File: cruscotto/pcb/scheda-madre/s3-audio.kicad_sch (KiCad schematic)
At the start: 11 parts, among them J10 Verso P1 S3: 5V TXD RXD GND, J11 Verso P2 S3: IO19 IO11 IO12 I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, J12 Verso P6 Speak S3, K1 G2RL-2 DC5, K2 G2RL-2 DC5, Q9 AO3400A

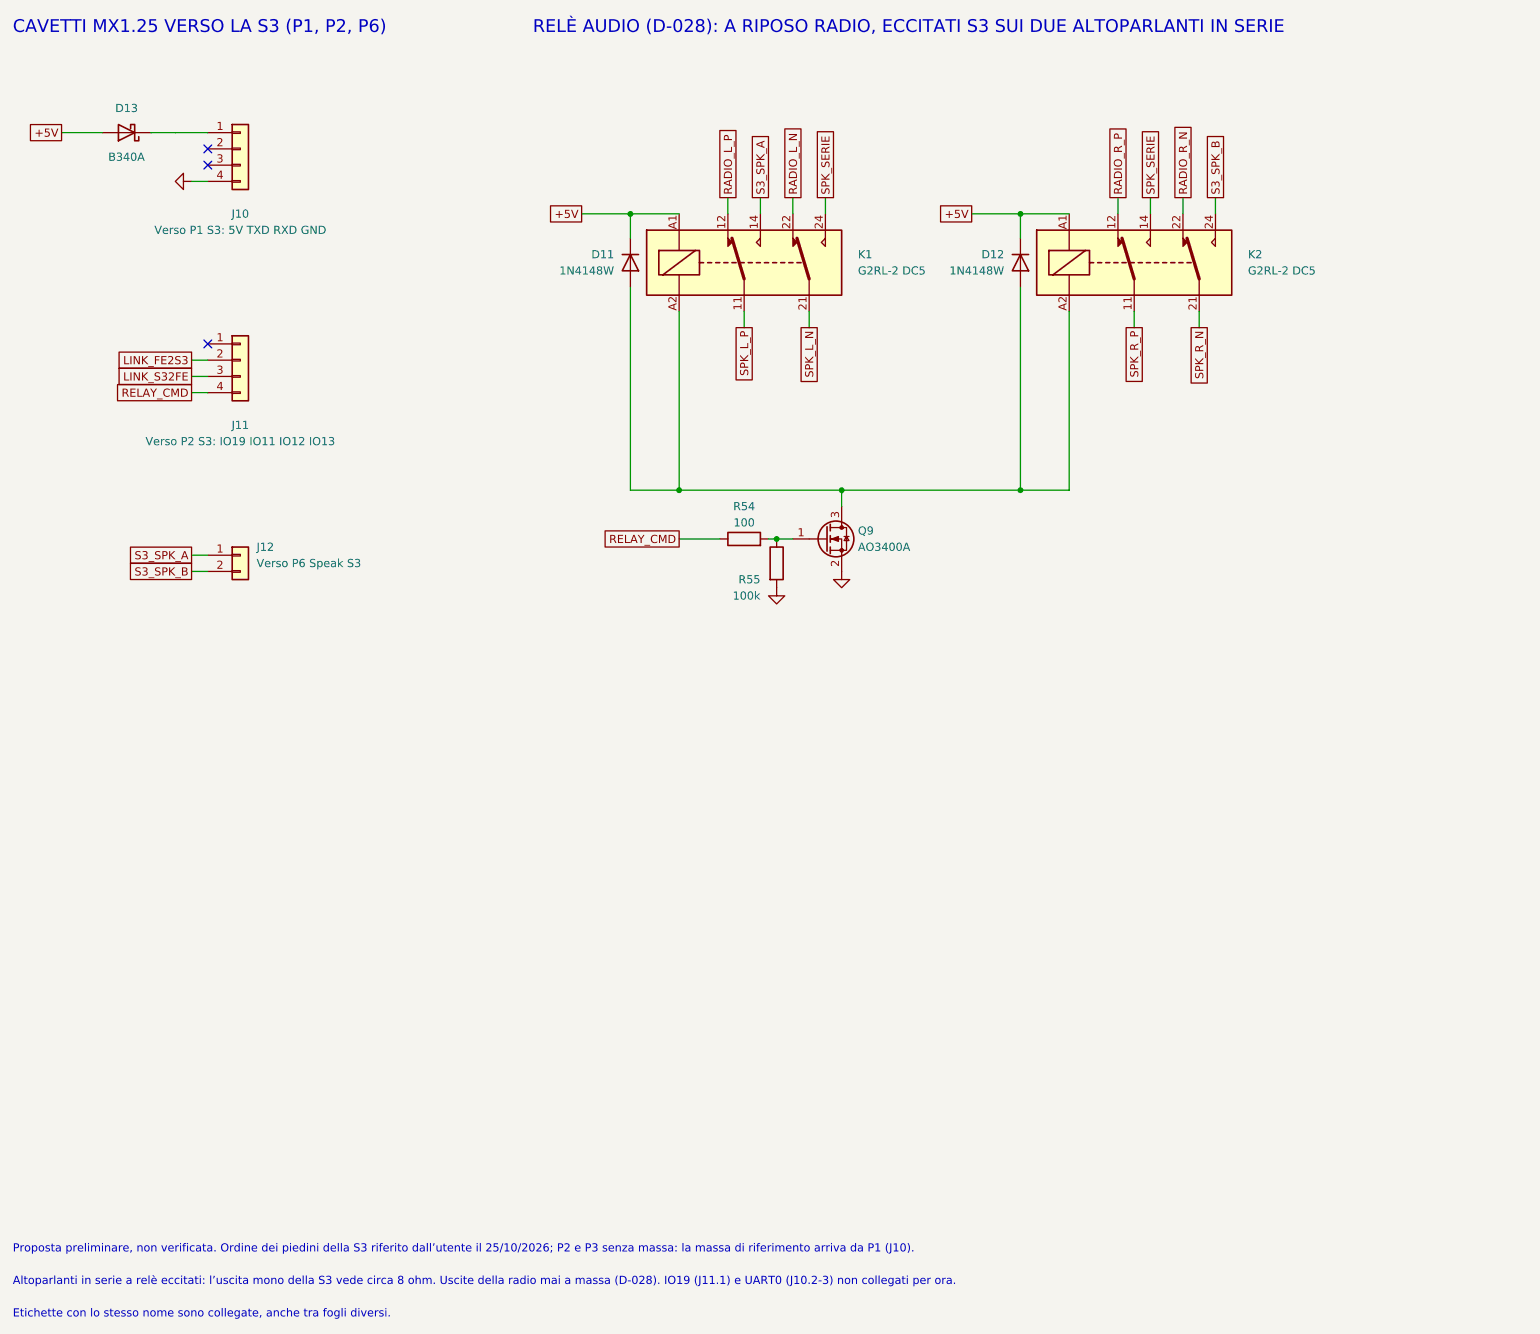
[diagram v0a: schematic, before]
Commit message: feat(schematic): D-054 dashboard buttons, S1 to S3 IO19 and S2 to front-end GPIO5
S1/S2 symbols match the PCB switches; GPIO5 pull-up 10k; GPIO table and S3 connector table updated. 97 nets checked, ERC 0 errors.

Co-Authored-By: Claude Opus 5.5 <noreply@anthropic.com>
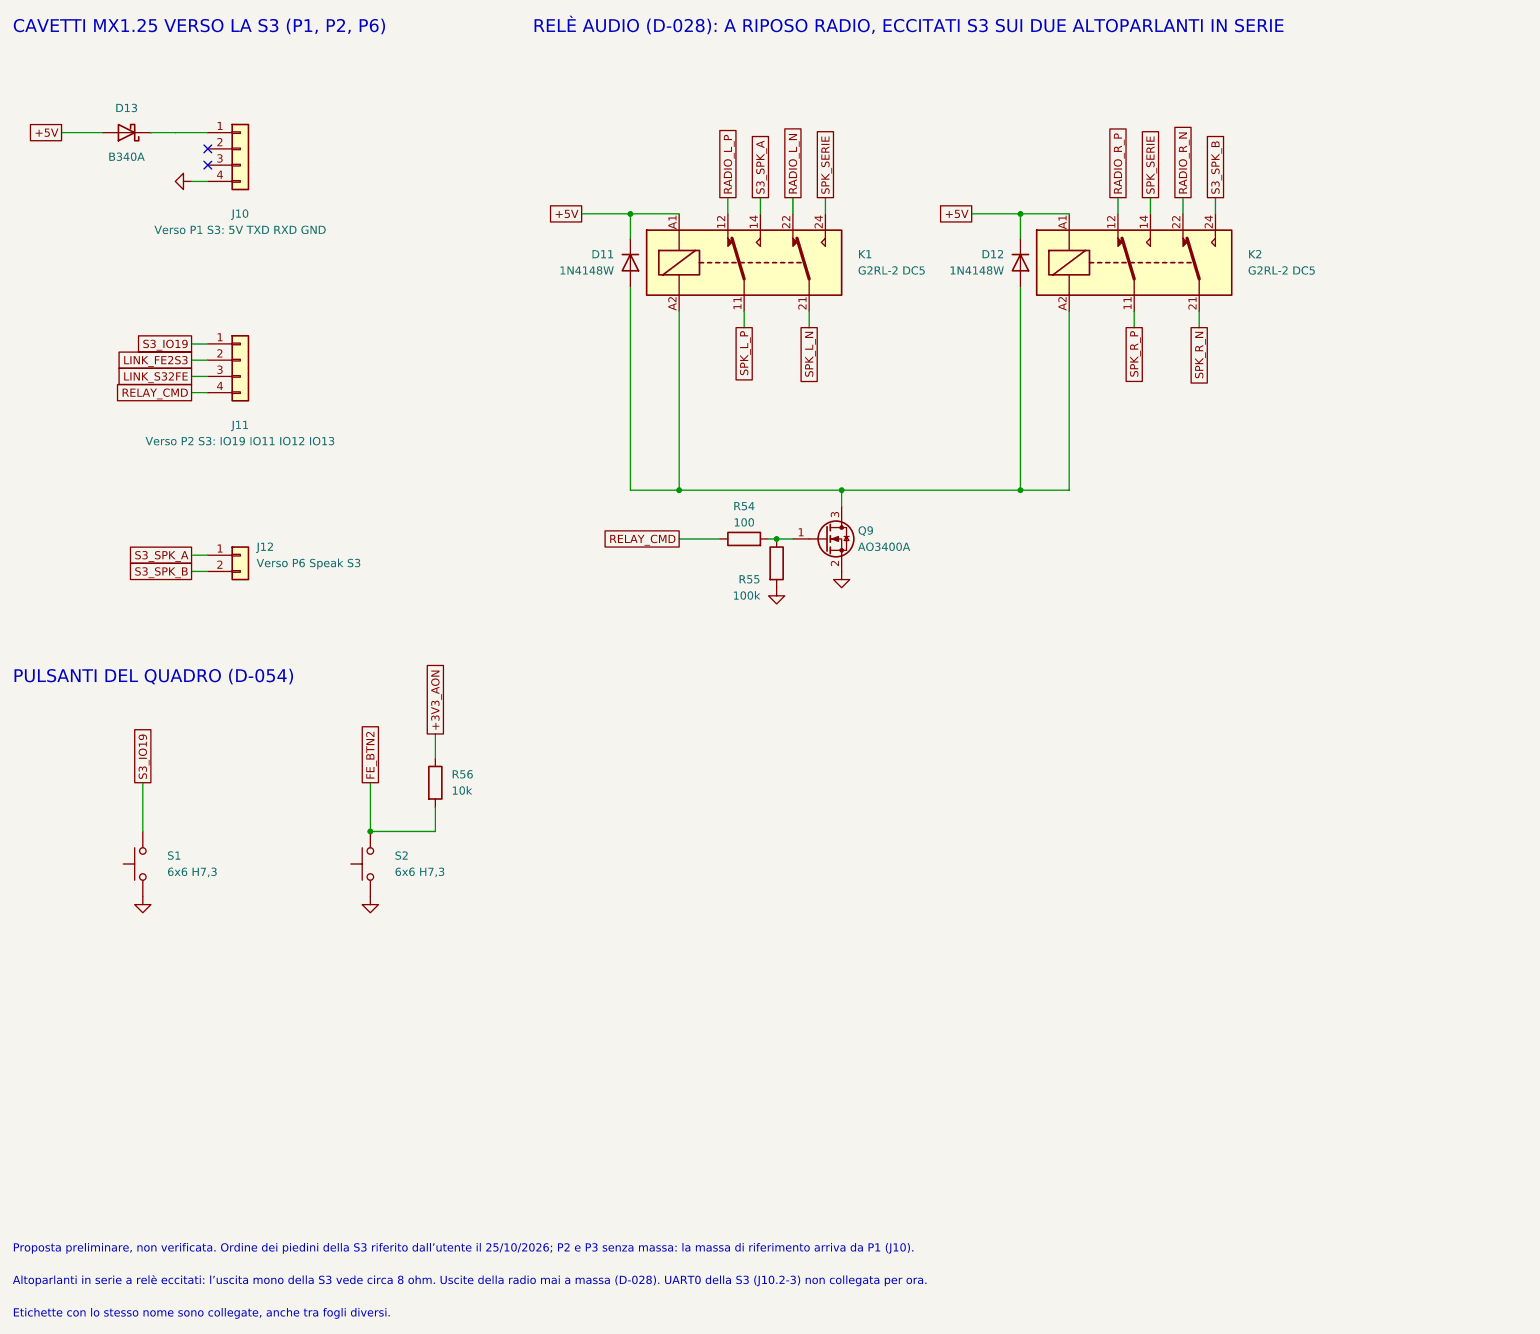
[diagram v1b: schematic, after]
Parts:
- added R56: 10k, Resistor_SMD:R_0805_2012Metric_Pad1.20x1.40mm_HandSolder, symbol Device:R
- added S1, S2: 6x6 H7,3, Button_Switch_THT:SW_PUSH_6mm_H7.3mm, symbol Switch:SW_Push
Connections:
- net GND: now also S1.1, S2.1
- net S3_IO19: now reaches J11.1 (Pin_1)
- net S3_IO19: now also S1.2
- new net +3V3_AON: R56.1
- new net FE_BTN2: R56.2, S2.2
- no-connect marks 3 -> 2
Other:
- note added: "Altoparlanti in serie a relè eccitati: l’uscita mono della S3 vede circa 8 ohm. Uscite della radio mai a massa (D-028). UART0 della S3 (J10.2-3) non collegata per ora."
- note added: "PULSANTI DEL QUADRO (D-054)"
- note removed: "Altoparlanti in serie a relè eccitati: l’uscita mono della S3 vede circa 8 ohm. Uscite della radio mai a massa (D-028). IO19 (J11.1) e UART0 (J10.2-3) non collegati per ora."
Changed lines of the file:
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@@
 		(instances (project "scheda-madre" (path "/ccee1fe6-cbff-5665-be3b-629f18d22eb3/37bc7f39-e7e3-500a-8f0b-bbc32f15f7b4" (reference "J11") (unit 1))))
 	)
-	(no_connect (at 55.88 93.98))
+	(wire (pts (xy 55.88 93.98) (xy 53.34 93.98)) (stroke (width 0) (type default)))
+	(global_label "S3_IO19" (shape passive) (at 53.34 93.98 180) (fields_autoplaced yes) (effects (font (size 1.27 1.27)) (justify right))
+		(property "Intersheetrefs" "${INTERSHEET_REFS}" (at 53.34 93.98 0) (effects (font (size 1.27 1.27)) (justify right) (hide yes))))
 	(wire (pts (xy 55.88 96.52) (xy 53.34 96.52)) (stroke (width 0) (type default)))
 	(global_label "LINK_FE2S3" (shape passive) (at 53.34 96.52 180) (fields_autoplaced yes) (effects (font (size 1.27 1.27)) (justify right))
@@
 	(global_label "RELAY_CMD" (shape passive) (at 129.54 124.46 180) (fields_autoplaced yes) (effects (font (size 1.27 1.27)) (justify right))
 		(property "Intersheetrefs" "${INTERSHEET_REFS}" (at 129.54 124.46 0) (effects (font (size 1.27 1.27)) (justify right) (hide yes))))
+	(symbol (lib_id "Switch:SW_Push") (at 45.72 175.26 90) (unit 1) (exclude_from_sim no) (in_bom yes) (on_board yes) (dnp no)
+		(property "Reference" "S1" (at 49.53 173.99 90) (effects (font (size 1.27 1.27)) (justify right)))
+		(property "Value" "6x6 H7,3" (at 49.53 176.53 90) (effects (font (size 1.27 1.27)) (justify right)))
+		(property "Footprint" "Button_Switch_THT:SW_PUSH_6mm_H7.3mm" (at 45.72 175.26 0) (hide yes) (effects (font (size 1.27 1.27))))
+		(property "Datasheet" "" (at 45.72 175.26 0) (hide yes) (effects (font (size 1.27 1.27))))
+		(property "Description" "Pulsante sinistro: IO19 della S3 (emergenza D-039, cambio pagina); pull-up interno della S3" (at 45.72 175.26 0) (hide yes) (effects (font (size 1.27 1.27))))
+		(pin "1")
+		(pin "2")
+		(instances (project "scheda-madre" (path "/ccee1fe6-cbff-5665-be3b-629f18d22eb3/37bc7f39-e7e3-500a-8f0b-bbc32f15f7b4" (reference "S1") (unit 1))))
+	)
+	(symbol (lib_id "power:GND") (at 45.72 180.34 0) (unit 1) (exclude_from_sim no) (in_bom no) (on_board no) (dnp no)
+		(property "Reference" "#PWR095" (at 45.72 173.99 0) (hide yes) (effects (font (size 1.27 1.27))))
+		(property "Value" "GND" (at 45.72 176.53 0) (hide yes) (effects (font (size 1.27 1.27))))
+		(property "Footprint" "" (at 45.72 180.34 0) (hide yes) (effects (font (size 1.27 1.27))))
+		(property "Datasheet" "" (at 45.72 180.34 0) (hide yes) (effects (font (size 1.27 1.27))))
+		(property "Description" "" (at 45.72 180.34 0) (hide yes) (effects (font (size 1.27 1.27))))
+		(pin "1")
+		(instances (project "scheda-madre" (path "/ccee1fe6-cbff-5665-be3b-629f18d22eb3/37bc7f39-e7e3-500a-8f0b-bbc32f15f7b4" (reference "#PWR095") (unit 1))))
+	)
+	(wire (pts (xy 45.72 170.18) (xy 45.72 162.56)) (stroke (width 0) (type default)))
+	(global_label "S3_IO19" (shape passive) (at 45.72 162.56 90) (fields_autoplaced yes) (effects (font (size 1.27 1.27)) (justify left))
+		(property "Intersheetrefs" "${INTERSHEET_REFS}" (at 45.72 162.56 0) (effects (font (size 1.27 1.27)) (justify left) (hide yes))))
+	(symbol (lib_id "Switch:SW_Push") (at 81.28 175.26 90) (unit 1) (exclude_from_sim no) (in_bom yes) (on_board yes) (dnp no)
+		(property "Reference" "S2" (at 85.09 173.99 90) (effects (font (size 1.27 1.27)) (justify right)))
+		(property "Value" "6x6 H7,3" (at 85.09 176.53 90) (effects (font (size 1.27 1.27)) (justify right)))
+		(property "Footprint" "Button_Switch_THT:SW_PUSH_6mm_H7.3mm" (at 81.28 175.26 0) (hide yes) (effects (font (size 1.27 1.27))))
+		(property "Datasheet" "" (at 81.28 175.26 0) (hide yes) (effects (font (size 1.27 1.27))))
+		(property "Description" "Pulsante destro: GPIO5 del front-end, pull-up R56" (at 81.28 175.26 0) (hide yes) (effects (font (size 1.27 1.27))))
+		(pin "1")
+		(pin "2")
+		(instances (project "scheda-madre" (path "/ccee1fe6-cbff-5665-be3b-629f18d22eb3/37bc7f39-e7e3-500a-8f0b-bbc32f15f7b4" (reference "S2") (unit 1))))
+	)
+	(symbol (lib_id "power:GND") (at 81.28 180.34 0) (unit 1) (exclude_from_sim no) (in_bom no) (on_board no) (dnp no)
+		(property "Reference" "#PWR096" (at 81.28 173.99 0) (hide yes) (effects (font (size 1.27 1.27))))
+		(property "Value" "GND" (at 81.28 176.53 0) (hide yes) (effects (font (size 1.27 1.27))))
+		(property "Footprint" "" (at 81.28 180.34 0) (hide yes) (effects (font (size 1.27 1.27))))
+		(property "Datasheet" "" (at 81.28 180.34 0) (hide yes) (effects (font (size 1.27 1.27))))
+		(property "Description" "" (at 81.28 180.34 0) (hide yes) (effects (font (size 1.27 1.27))))
+		(pin "1")
+		(instances (project "scheda-madre" (path "/ccee1fe6-cbff-5665-be3b-629f18d22eb3/37bc7f39-e7e3-500a-8f0b-bbc32f15f7b4" (reference "#PWR096") (unit 1))))
+	)
+	(wire (pts (xy 81.28 170.18) (xy 81.28 162.56)) (stroke (width 0) (type default)))
+	(global_label "FE_BTN2" (shape passive) (at 81.28 162.56 90) (fields_autoplaced yes) (effects (font (size 1.27 1.27)) (justify left))
+		(property "Intersheetrefs" "${INTERSHEET_REFS}" (at 81.28 162.56 0) (effects (font (size 1.27 1.27)) (justify left) (hide yes))))
+	(symbol (lib_id "Device:R") (at 91.44 162.56 0) (unit 1) (exclude_from_sim no) (in_bom yes) (on_board yes) (dnp no)
+		(property "Reference" "R56" (at 93.98 161.29 0) (effects (font (size 1.27 1.27)) (justify left)))
+		(property "Value" "10k" (at 93.98 163.83 0) (effects (font (size 1.27 1.27)) (justify left)))
+		(property "Footprint" "Resistor_SMD:R_0805_2012Metric_Pad1.20x1.40mm_HandSolder" (at 91.44 162.56 0) (hide yes) (effects (font (size 1.27 1.27))))
+		(property "Datasheet" "" (at 91.44 162.56 0) (hide yes) (effects (font (size 1.27 1.27))))
+		(property "Description" "GPIO5 è un pin di avvio: alto a riposo, come richiesto" (at 91.44 162.56 0) (hide yes) (effects (font (size 1.27 1.27))))
+		(pin "1")
+		(pin "2")
+		(instances (project "scheda-madre" (path "/ccee1fe6-cbff-5665-be3b-629f18d22eb3/37bc7f39-e7e3-500a-8f0b-bbc32f15f7b4" (reference "R56") (unit 1))))
+	)
+	(wire (pts (xy 91.44 158.75) (xy 91.44 154.94)) (stroke (width 0) (type default)))
+	(global_label "+3V3_AON" (shape passive) (at 91.44 154.94 90) (fields_autoplaced yes) (effects (font (size 1.27 1.27)) (justify left))
+		(property "Intersheetrefs" "${INTERSHEET_REFS}" (at 91.44 154.94 0) (effects (font (size 1.27 1.27)) (justify left) (hide yes))))
+	(wire (pts (xy 91.44 166.37) (xy 91.44 170.18)) (stroke (width 0) (type default)))
+	(wire (pts (xy 91.44 170.18) (xy 81.28 170.18)) (stroke (width 0) (type default)))
+	(text "PULSANTI DEL QUADRO (D-054)" (exclude_from_sim no) (at 25.4 147.32 0) (effects (font (size 2.0 2.0)) (justify left bottom)))
 	(text "CAVETTI MX1.25 VERSO LA S3 (P1, P2, P6)" (exclude_from_sim no) (at 25.4 45.72 0) (effects (font (size 2.0 2.0)) (justify left bottom)))
 	(text "RELÈ AUDIO (D-028): A RIPOSO RADIO, ECCITATI S3 SUI DUE ALTOPARLANTI IN SERIE" (exclude_from_sim no) (at 106.68 45.72 0) (effects (font (size 2.0 2.0)) (justify left bottom)))
 	(text "Proposta preliminare, non verificata. Ordine dei piedini della S3 riferito dall’utente il 25/10/2026; P2 e P3 senza massa: la massa di riferimento arriva da P1 (J10)." (exclude_from_sim no) (at 25.4 236.22 0) (effects (font (size 1.27 1.27)) (justify left bottom)))
-	(text "Altoparlanti in serie a relè eccitati: l’uscita mono della S3 vede circa 8 ohm. Uscite della radio mai a massa (D-028). IO19 (J11.1) e UART0 (J10.2-3) non collegati per ora." (exclude_from_sim no) (at 25.4 241.3 0) (effects (font (size 1.27 1.27)) (justify left bottom)))
+	(text "Altoparlanti in serie a relè eccitati: l’uscita mono della S3 vede circa 8 ohm. Uscite della radio mai a massa (D-028). UART0 della S3 (J10.2-3) non collegata per ora." (exclude_from_sim no) (at 25.4 241.3 0) (effects (font (size 1.27 1.27)) (justify left bottom)))
 	(text "Etichette con lo stesso nome sono collegate, anche tra fogli diversi." (exclude_from_sim no) (at 25.4 246.38 0) (effects (font (size 1.27 1.27)) (justify left bottom)))
+	(junction (at 81.28 170.18) (diameter 0) (color 0 0 0 0))
 	(junction (at 121.92 73.66) (diameter 0) (color 0 0 0 0))
 	(junction (at 129.54 116.84) (diameter 0) (color 0 0 0 0))

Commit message: feat(pcb): S3 cable connectors mirrored to face their S3 counterparts, right-angle PicoBlade; height check
KiCad F view is the mirror of the user's DXF (seen from the rear): S3-related parts placed at negative x. Right-angle PicoBlade 53048 keeps plugs flat. Clearance to the S3 at least 5.5 mm on face F. Relays moved to the left back, IMU socket to the right.

Co-Authored-By: Claude Opus 5.5 <noreply@anthropic.com>
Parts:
- J10, J11: footprint Connector_Molex:Molex_PicoBlade_53047-0410_1x04_P1.25mm_Vertical -> Connector_Molex:Molex_PicoBlade_53048-0410_1x04_P1.25mm_Horizontal
- J12: footprint Connector_Molex:Molex_PicoBlade_53047-0210_1x02_P1.25mm_Vertical -> Connector_Molex:Molex_PicoBlade_53048-0210_1x02_P1.25mm_Horizontal
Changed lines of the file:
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@@
 		(property "Reference" "J10" (at 60.96 73.66 0) (effects (font (size 1.27 1.27))))
 		(property "Value" "Verso P1 S3: 5V TXD RXD GND" (at 60.96 76.2 0) (effects (font (size 1.27 1.27))))
-		(property "Footprint" "Connector_Molex:Molex_PicoBlade_53047-0410_1x04_P1.25mm_Vertical" (at 60.96 63.5 0) (hide yes) (effects (font (size 1.27 1.27))))
+		(property "Footprint" "Connector_Molex:Molex_PicoBlade_53048-0410_1x04_P1.25mm_Horizontal" (at 60.96 63.5 0) (hide yes) (effects (font (size 1.27 1.27))))
 		(property "Datasheet" "" (at 60.96 63.5 0) (hide yes) (effects (font (size 1.27 1.27))))
 		(property "Description" "P1 dal basso verso l’alto 5V, TXD, RXD, GND; UART0 della S3 non usata (riserva per la porta nascosta)" (at 60.96 63.5 0) (hide yes) (effects (font (size 1.27 1.27))))
@@
 		(property "Reference" "J11" (at 60.96 106.68 0) (effects (font (size 1.27 1.27))))
 		(property "Value" "Verso P2 S3: IO19 IO11 IO12 IO13" (at 60.96 109.22 0) (effects (font (size 1.27 1.27))))
-		(property "Footprint" "Connector_Molex:Molex_PicoBlade_53047-0410_1x04_P1.25mm_Vertical" (at 60.96 96.52 0) (hide yes) (effects (font (size 1.27 1.27))))
+		(property "Footprint" "Connector_Molex:Molex_PicoBlade_53048-0410_1x04_P1.25mm_Horizontal" (at 60.96 96.52 0) (hide yes) (effects (font (size 1.27 1.27))))
 		(property "Datasheet" "" (at 60.96 96.52 0) (hide yes) (effects (font (size 1.27 1.27))))
 		(property "Description" "P2 da destra a sinistra IO19, IO11, IO12, IO13; P2 non porta massa: riferimento da J10 (P1)" (at 60.96 96.52 0) (hide yes) (effects (font (size 1.27 1.27))))
@@
 		(property "Reference" "J12" (at 63.5 125.73 0) (effects (font (size 1.27 1.27)) (justify left)))
 		(property "Value" "Verso P6 Speak S3" (at 63.5 128.27 0) (effects (font (size 1.27 1.27)) (justify left)))
-		(property "Footprint" "Connector_Molex:Molex_PicoBlade_53047-0210_1x02_P1.25mm_Vertical" (at 60.96 127 0) (hide yes) (effects (font (size 1.27 1.27))))
+		(property "Footprint" "Connector_Molex:Molex_PicoBlade_53048-0210_1x02_P1.25mm_Horizontal" (at 60.96 127 0) (hide yes) (effects (font (size 1.27 1.27))))
 		(property "Datasheet" "" (at 60.96 127 0) (hide yes) (effects (font (size 1.27 1.27))))
 		(property "Description" "Uscita differenziale senza indicazione di polarità: nessun filo a massa, fase da verificare all’ascolto" (at 60.96 127 0) (hide yes) (effects (font (size 1.27 1.27))))
